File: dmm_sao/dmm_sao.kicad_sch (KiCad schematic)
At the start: 6 parts, among them SW1 TS5220A, SW2 RotaryEncoder, X1 Badgelife_sao_connector_v169b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

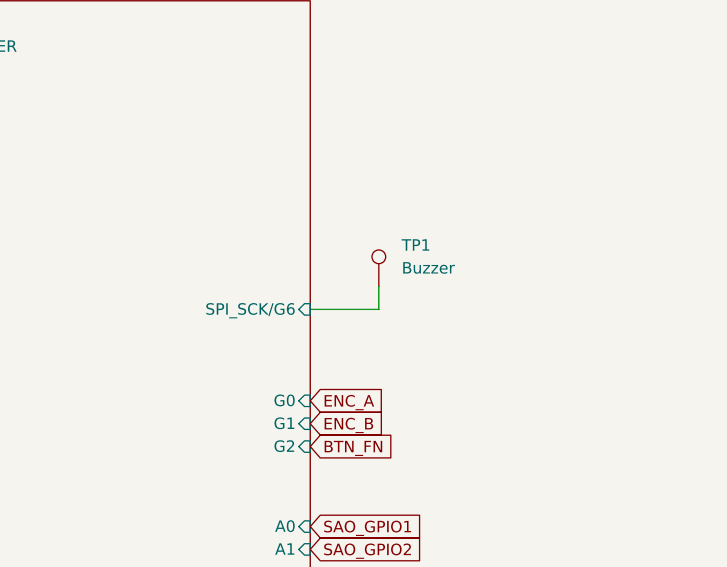
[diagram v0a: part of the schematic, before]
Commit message: Moved buzzer to base board
Also:
- Moved a few parts to make space for the buzzer
- Connected the buzzer in a push/pull setup for better volume
- Changed the edgecut a little, to have better space for knob intent mechanism in case
- Tweaked pads for spring loaded pins to match manufacturer suggestion
- Made the paste for the display connector 10% smaller

Signed-off-by: Thomas Flummer <tf@flummer.net>
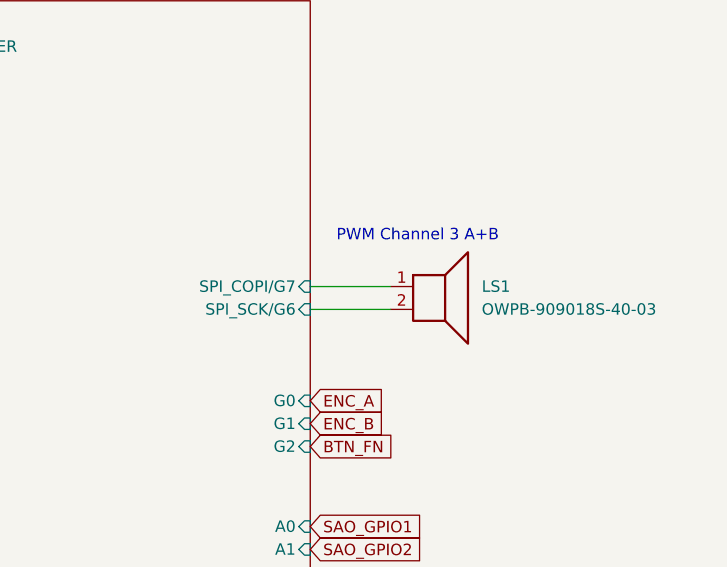
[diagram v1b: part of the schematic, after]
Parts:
- removed TP1: Buzzer, TestPoint:TestPoint_Pad_D2.0mm, symbol Connector:TestPoint
- added LS1: OWPB-909018S-40-03, Buzzer_Beeper:Buzzer_CUI_CPT-9019S-SMT, symbol Device:Speaker
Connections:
- net RP2040/SPI_SCK/G6: now also LS1.2
- new net RP2040/SPI_COPI/G7: LS1.1
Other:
- sheet RP2040 ports: added SPI_COPI/G7; removed none
- note added: "PWM Channel 3 A+B"
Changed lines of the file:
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@@
 	(title_block
 		(title "DMM SAO")
-		(date "2024-10-05")
-		(rev "1.0")
+		(date "2024-11-19")
+		(rev "1.1")
 		(company "HXR.DK")
+		(comment 1 "CC-BY-SA")
+	)
+	(text "PWM Channel 3 A+B"
+		(exclude_from_sim no)
+		(at 251.968 64.262 0)
+		(effects
+			(font
+				(size 1.27 1.27)
+			)
+		)
 	)
 	(junction
@@
 	(wire
 		(pts
+			(xy 240.03 69.85) (xy 248.92 69.85)
+		)
+		(stroke
+			(width 0)
+			(type default)
+		)
+	)
+	(wire
+		(pts
 			(xy 189.23 142.24) (xy 189.23 137.16)
 		)
@@
 	(wire
 		(pts
-			(xy 240.03 72.39) (xy 247.65 72.39)
+			(xy 240.03 72.39) (xy 248.92 72.39)
 		)
 		(stroke
@@
 		(pts
 			(xy 157.48 111.76) (xy 152.4 111.76)
-		)
-		(stroke
-			(width 0)
-			(type default)
-		)
-	)
-	(wire
-		(pts
-			(xy 247.65 72.39) (xy 247.65 69.85)
 		)
 		(stroke
@@
 	)
 	(symbol
-		(lib_id "Connector:TestPoint")
-		(at 247.65 69.85 0)
+		(lib_id "Device:Speaker")
+		(at 254 69.85 0)
 		(unit 1)
 		(exclude_from_sim no)
@@
 		(dnp no)
 		(fields_autoplaced yes)
-		(property "Reference" "TP1"
-			(at 250.19 65.2779 0)
-			(effects
-				(font
-					(size 1.27 1.27)
-				)
-				(justify left)
-			)
-		)
-		(property "Value" "Buzzer"
-			(at 250.19 67.8179 0)
-			(effects
-				(font
-					(size 1.27 1.27)
-				)
-				(justify left)
-			)
-		)
-		(property "Footprint" "TestPoint:TestPoint_Pad_D2.0mm"
-			(at 252.73 69.85 0)
+		(property "Reference" "LS1"
+			(at 259.08 69.8499 0)
+			(effects
+				(font
+					(size 1.27 1.27)
+				)
+				(justify left)
+			)
+		)
+		(property "Value" "OWPB-909018S-40-03"
+			(at 259.08 72.3899 0)
+			(effects
+				(font
+					(size 1.27 1.27)
+				)
+				(justify left)
+			)
+		)
+		(property "Footprint" "Buzzer_Beeper:Buzzer_CUI_CPT-9019S-SMT"
+			(at 254 74.93 0)
 			(effects
 				(font
@@
 		)
 		(property "Datasheet" "~"
-			(at 252.73 69.85 0)
-			(effects
-				(font
-					(size 1.27 1.27)
-				)
-				(hide yes)
-			)
-		)
-		(property "Description" "test point"
-			(at 247.65 69.85 0)
+			(at 253.746 71.12 0)
+			(effects
+				(font
+					(size 1.27 1.27)
+				)
+				(hide yes)
+			)
+		)
+		(property "Description" "Speaker"
+			(at 254 69.85 0)
 			(effects
 				(font
@@
 		)
 		(pin "1"
+		)
+		(pin "2"
 		)
 		(instances
 			(project ""
 				(path "/f26ce819-5d33-4e93-ae51-f48c2c0f5bc2"
-					(reference "TP1")
+					(reference "LS1")
 					(unit 1)
 				)
@@
 			(effects
 				(font
+					(size 1.27 1.27)
+				)
+				(justify right)
+			)
+		)
+		(pin "SPI_COPI{slash}G7" input
+			(at 240.03 69.85 0)
+			(effects
+				(font
